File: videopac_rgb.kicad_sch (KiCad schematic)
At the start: 37 parts, among them J1 RGB Input, J2 DAC Output, Q1 BC558, Q2 BC548, Q3 BC558, Q4 BC548, Q5 BC558, Q6 BC548, Q7 BC548, U1 74HCT32

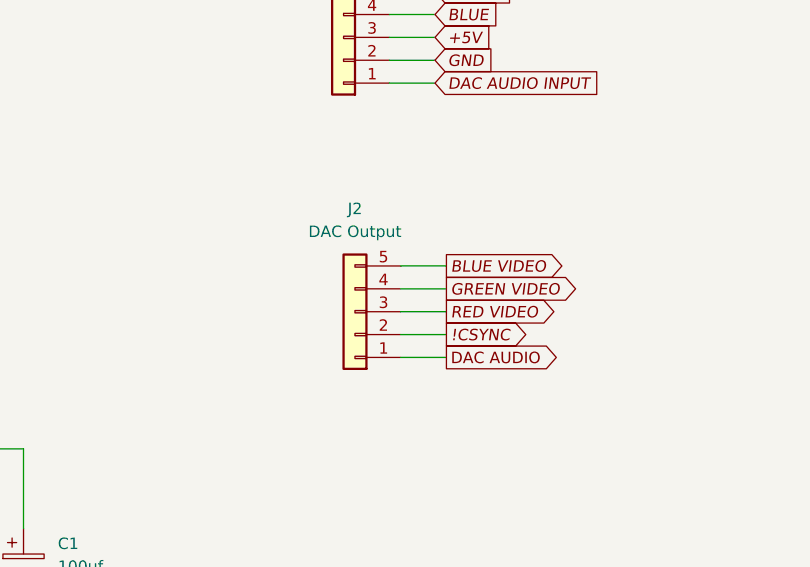
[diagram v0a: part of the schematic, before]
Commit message: Add additional ground connection.
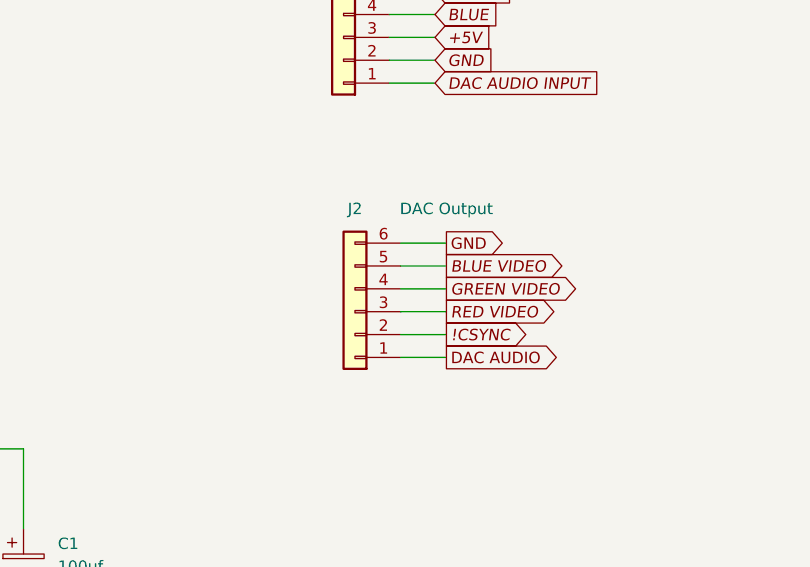
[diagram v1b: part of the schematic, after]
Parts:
- J2: footprint Connector_PinHeader_2.54mm:PinHeader_1x05_P2.54mm_Horizontal -> Connector_PinHeader_2.54mm:PinHeader_1x06_P2.54mm_Horizontal; symbol Connector_Generic:Conn_01x05 -> Connector_Generic:Conn_01x06
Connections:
- net GND: now also J2.6 (Pin_6)
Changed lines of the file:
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@@
+    (stroke (width 0) (type default) (color 0 0 0 0))
+  )
+  (wire (pts (xy 231.14 69.85) (xy 236.22 69.85))
     (stroke (width 0) (type default) (color 0 0 0 0))
   )
@@
     (effects (font (size 1.27 1.27)) (justify left))
     (property "Intersheet References" "${INTERSHEET_REFS}" (id 0) (at 85.3864 162.4806 0)
+      (effects (font (size 1.27 1.27)) (justify left) hide)
+    )
+  )
+  (global_label "GND" (shape output) (at 236.22 69.85 0) (fields_autoplaced)
+    (effects (font (size 1.27 1.27)) (justify left))
+    (property "Intersheet References" "${INTERSHEET_REFS}" (id 0) (at 242.5036 69.7706 0)
       (effects (font (size 1.27 1.27)) (justify left) hide)
     )
@@
     (pin "1")
   )
-  (symbol (lib_id "Connector_Generic:Conn_01x05") (at 226.06 77.47 180) (unit 1)
-    (in_bom yes) (on_board yes) (fields_autoplaced)
+  (symbol (lib_id "Connector_Generic:Conn_01x06") (at 226.06 77.47 180) (unit 1)
+    (in_bom yes) (on_board yes)
     (property "Reference" "J2" (id 0) (at 226.06 66.04 0))
-    (property "Value" "DAC Output" (id 1) (at 226.06 68.58 0))
-    (property "Footprint" "Connector_PinHeader_2.54mm:PinHeader_1x05_P2.54mm_Horizontal" (id 2) (at 226.06 77.47 0)
+    (property "Value" "DAC Output" (id 1) (at 236.22 66.04 0))
+    (property "Footprint" "Connector_PinHeader_2.54mm:PinHeader_1x06_P2.54mm_Horizontal" (id 2) (at 226.06 77.47 0)
       (effects (font (size 1.27 1.27)) hide)
     )
@@
     (pin "4")
     (pin "5")
+    (pin "6")
   )
   (symbol (lib_id "Device:R") (at 110.49 57.15 0) (unit 1)
@@
     )
     (path "/8099d792-a89f-449d-a9f4-345eff8d02ec"
-      (reference "J2") (unit 1) (value "DAC Output") (footprint "Connector_PinHeader_2.54mm:PinHeader_1x05_P2.54mm_Horizontal")
+      (reference "J2") (unit 1) (value "DAC Output") (footprint "Connector_PinHeader_2.54mm:PinHeader_1x06_P2.54mm_Horizontal")
     )
     (path "/3e213407-4fff-4911-b325-f46d096a19b9"
